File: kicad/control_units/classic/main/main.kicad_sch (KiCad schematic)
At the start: 21 parts, among them J1 Conn_01x04, J2 USB_C_Receptacle_USB2.0_14P, J3 Conn_01x05, J4 Conn_01x05, J5 Conn_01x05, J6 Conn_01x01, J7 Conn_01x01, SW1 SW_Push, U1 STM32C552CET6, U2 AZ1117CH2-3.3

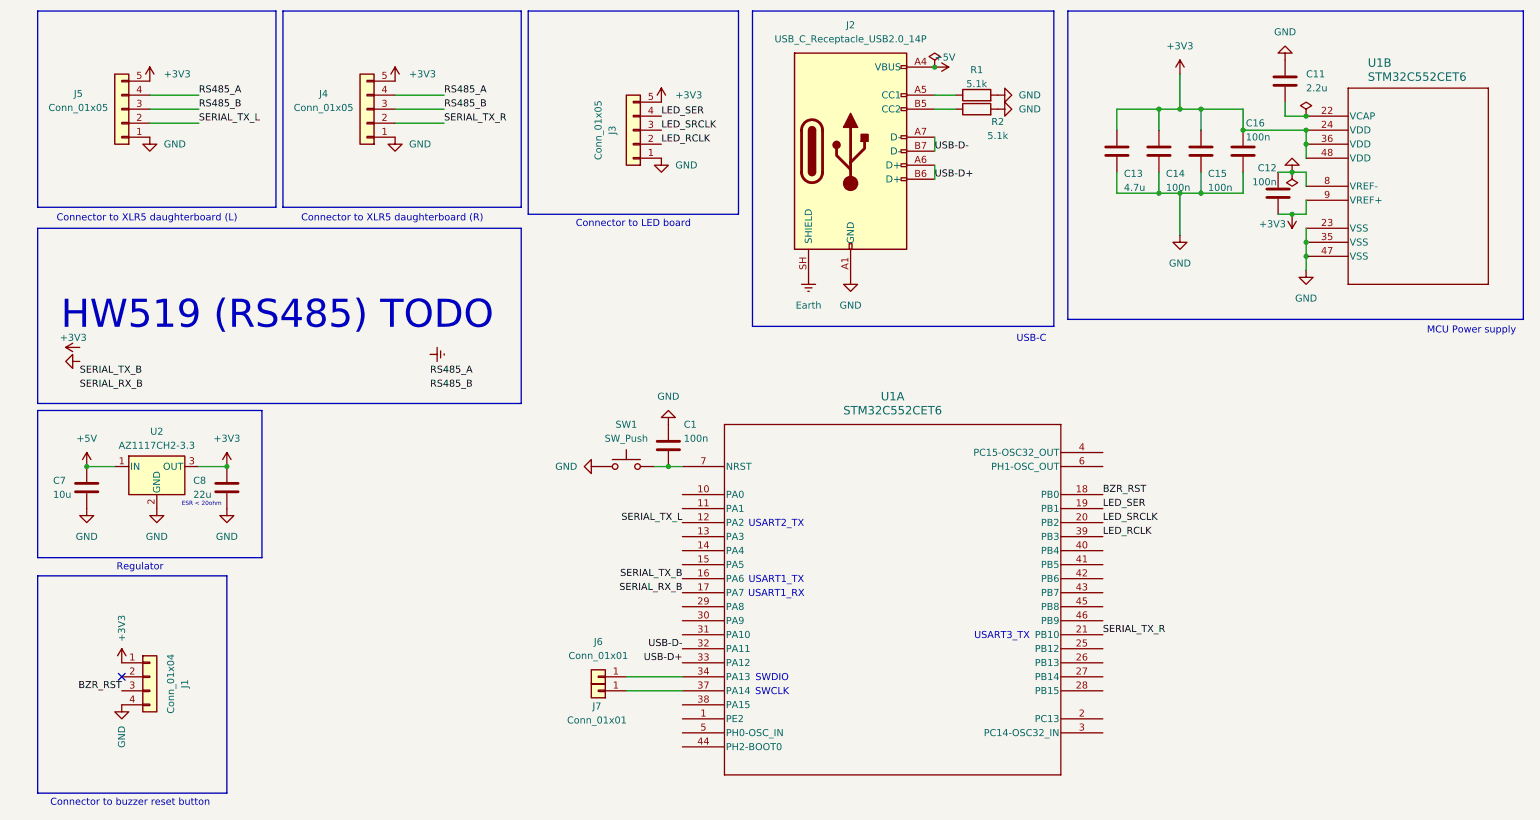
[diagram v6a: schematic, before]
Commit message: Added ESD protection for USB/RS485, not for serial lines yet; harmonised XLR pin numbers between boards
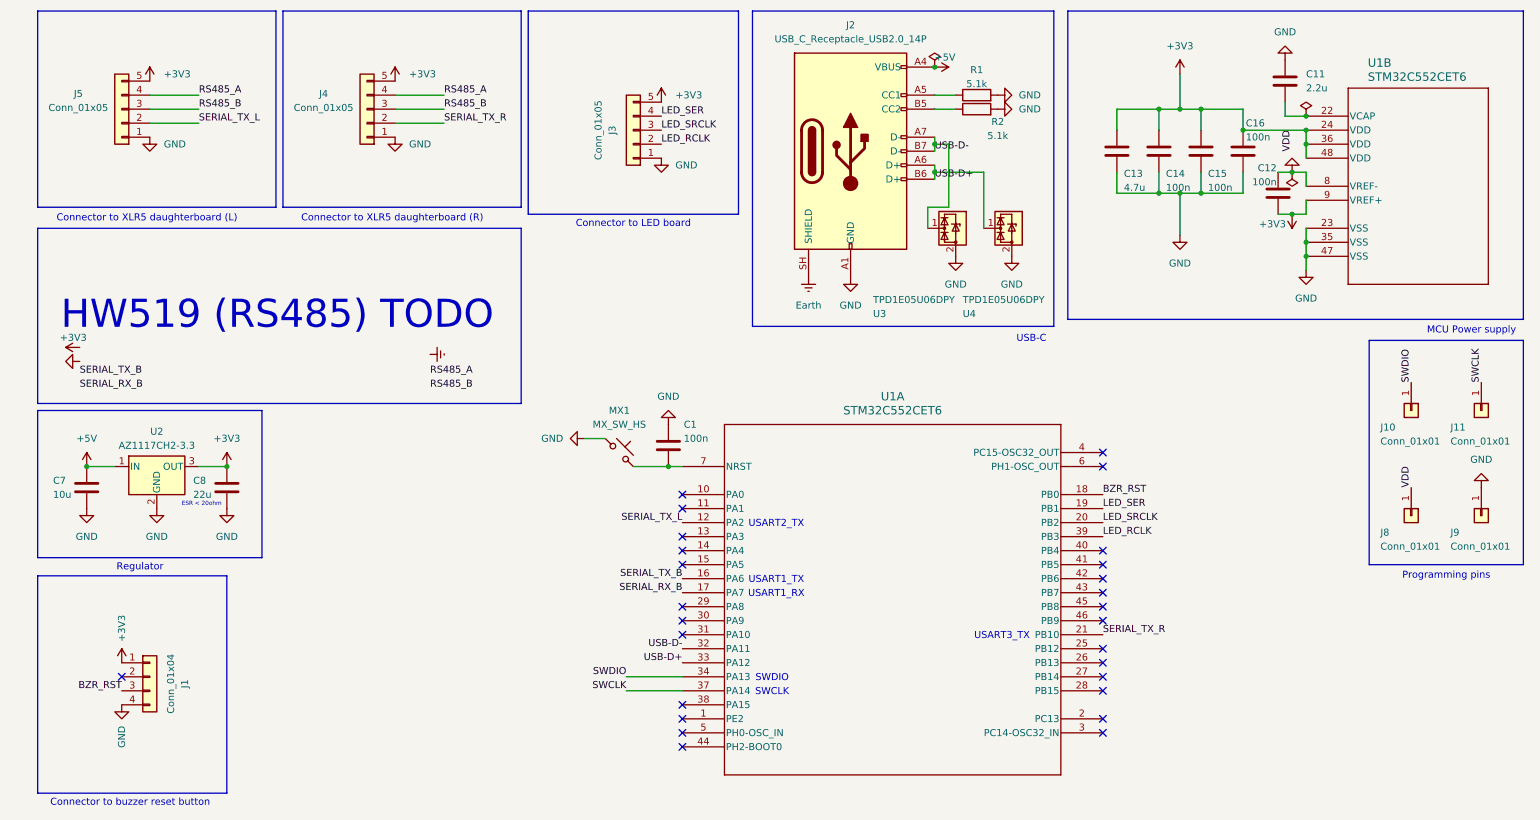
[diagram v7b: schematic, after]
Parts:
- removed J6, J7: Conn_01x01, symbol Connector_Generic:Conn_01x01
- removed SW1: SW_Push, symbol Switch:SW_Push
- added J10, J11, J8, J9: Conn_01x01, symbol Connector_Generic:Conn_01x01
- added MX1: MX_SW_HS, PCM_marbastlib-mx:SW_MX_HS_CPG151101S11_1u, symbol marbastlib-mx:MX_SW_HS_CPG151101S11
- added U3, U4: TPD1E05U06DPY, Package_SON:Texas_DPY0002A_0.6x1mm_P0.65mm, symbol Power_Protection:TPD1E05U06DPY
- C1, C11, C12, C13, C14, C15, C16, C7, C8: footprint (none) -> Capacitor_SMD:C_0805_2012Metric
- J2: footprint (none) -> Connector_USB:USB_C_Receptacle_Amphenol_12401610E4-2A
- R1, R2: footprint (none) -> Resistor_SMD:R_0805_2012Metric
- U1: footprint LQFP-48_STM -> Package_QFP:LQFP-48_7x7mm_P0.5mm
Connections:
- net +3V3: now also J8.1 (Pin_1)
- net GND: now also J9.1 (Pin_1), MX1.1, U3.2 (GND), U4.2 (GND)
- net USB-D+: now also U4.1 (I/O)
- net USB-D-: now also U3.1 (I/O)
- net SWDIO: now reaches U1.34 (PA13)
- net SWDIO: now also J10.1 (Pin_1)
- net SWCLK: now reaches U1.37 (PA14)
- net SWCLK: now also J11.1 (Pin_1)
- net at C1.2, U1.7 (NRST): now also MX1.2
- no-connect marks 1 -> 27
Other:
- note added: "Programming pins"

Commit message: Added some stuff for ESD protection on the serial lines; redid the STM32 programming pins
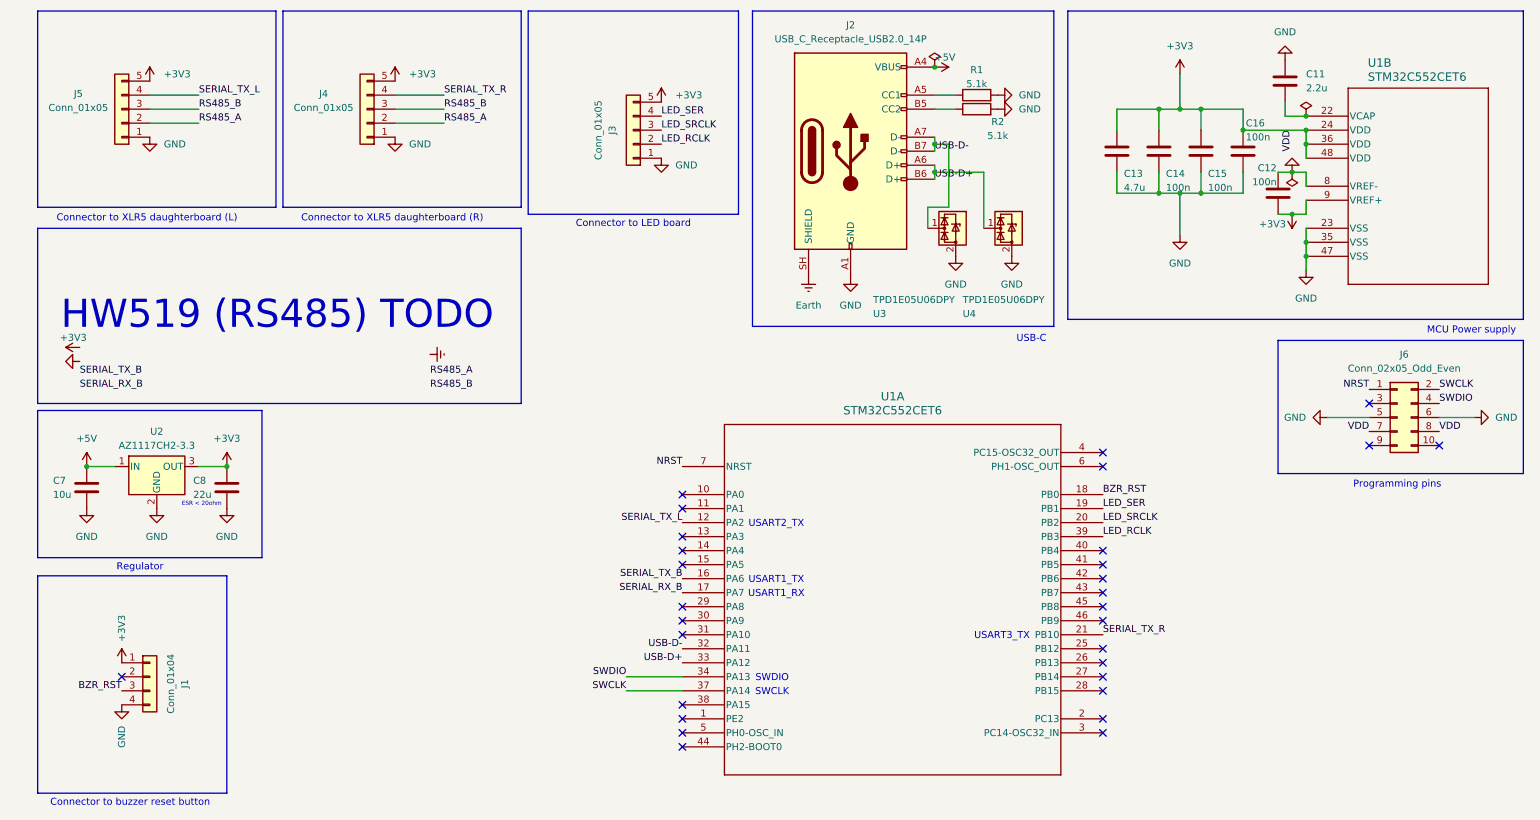
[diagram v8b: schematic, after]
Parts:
- removed C1: 100n, Capacitor_SMD:C_0805_2012Metric, symbol Device:C
- removed J10, J11, J8, J9: Conn_01x01, symbol Connector_Generic:Conn_01x01
- removed MX1: MX_SW_HS, PCM_marbastlib-mx:SW_MX_HS_CPG151101S11_1u, symbol marbastlib-mx:MX_SW_HS_CPG151101S11
- added J6: Conn_02x05_Odd_Even, symbol Connector_Generic:Conn_02x05_Odd_Even
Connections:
- net +3V3: now also J6.7 (Pin_7), J6.8 (Pin_8)
- net GND: now also J6.5 (Pin_5), J6.6 (Pin_6)
- net RS485_A: now also J4.2 (Pin_2), J5.2 (Pin_2); no longer J4.4 (Pin_4), J5.4 (Pin_4)
- net SERIAL_TX_L: now also J5.4 (Pin_4); no longer J5.2 (Pin_2)
- net SERIAL_TX_R: now also J4.4 (Pin_4); no longer J4.2 (Pin_2)
- net SWCLK: now also J6.2 (Pin_2)
- net SWDIO: now also J6.4 (Pin_4)
- net NRST: now reaches U1.7 (NRST)
- net NRST: now also J6.1 (Pin_1)
- no-connect marks 27 -> 30
